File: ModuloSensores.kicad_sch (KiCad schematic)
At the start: 12 parts, among them J27 Borner Ctrl. Empot. 1, J28 Borner Ctrl. Empot. 2, J29 Borner Ctrl. Polea, J30 Borner Capacitor 1, J31 Borner Capacitor 2, Q1 2N222, SW2 SW_SPDT, SW3 SW_SPDT, SW4 SW_SPDT

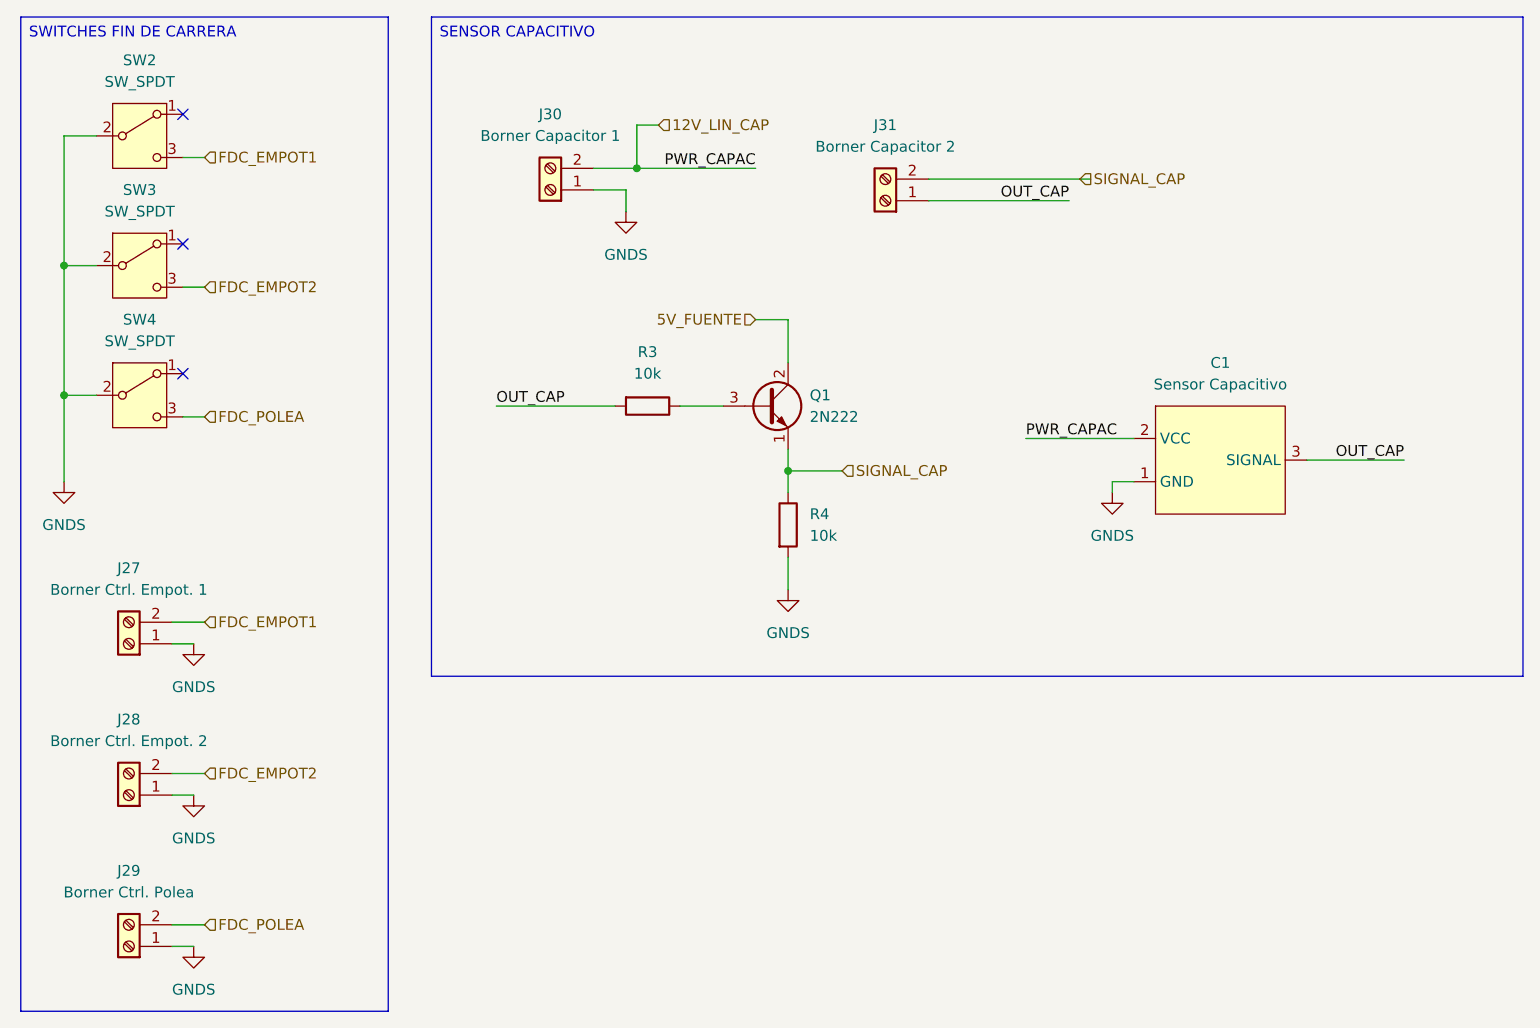
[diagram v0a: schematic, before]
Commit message: Version mandada para PCB
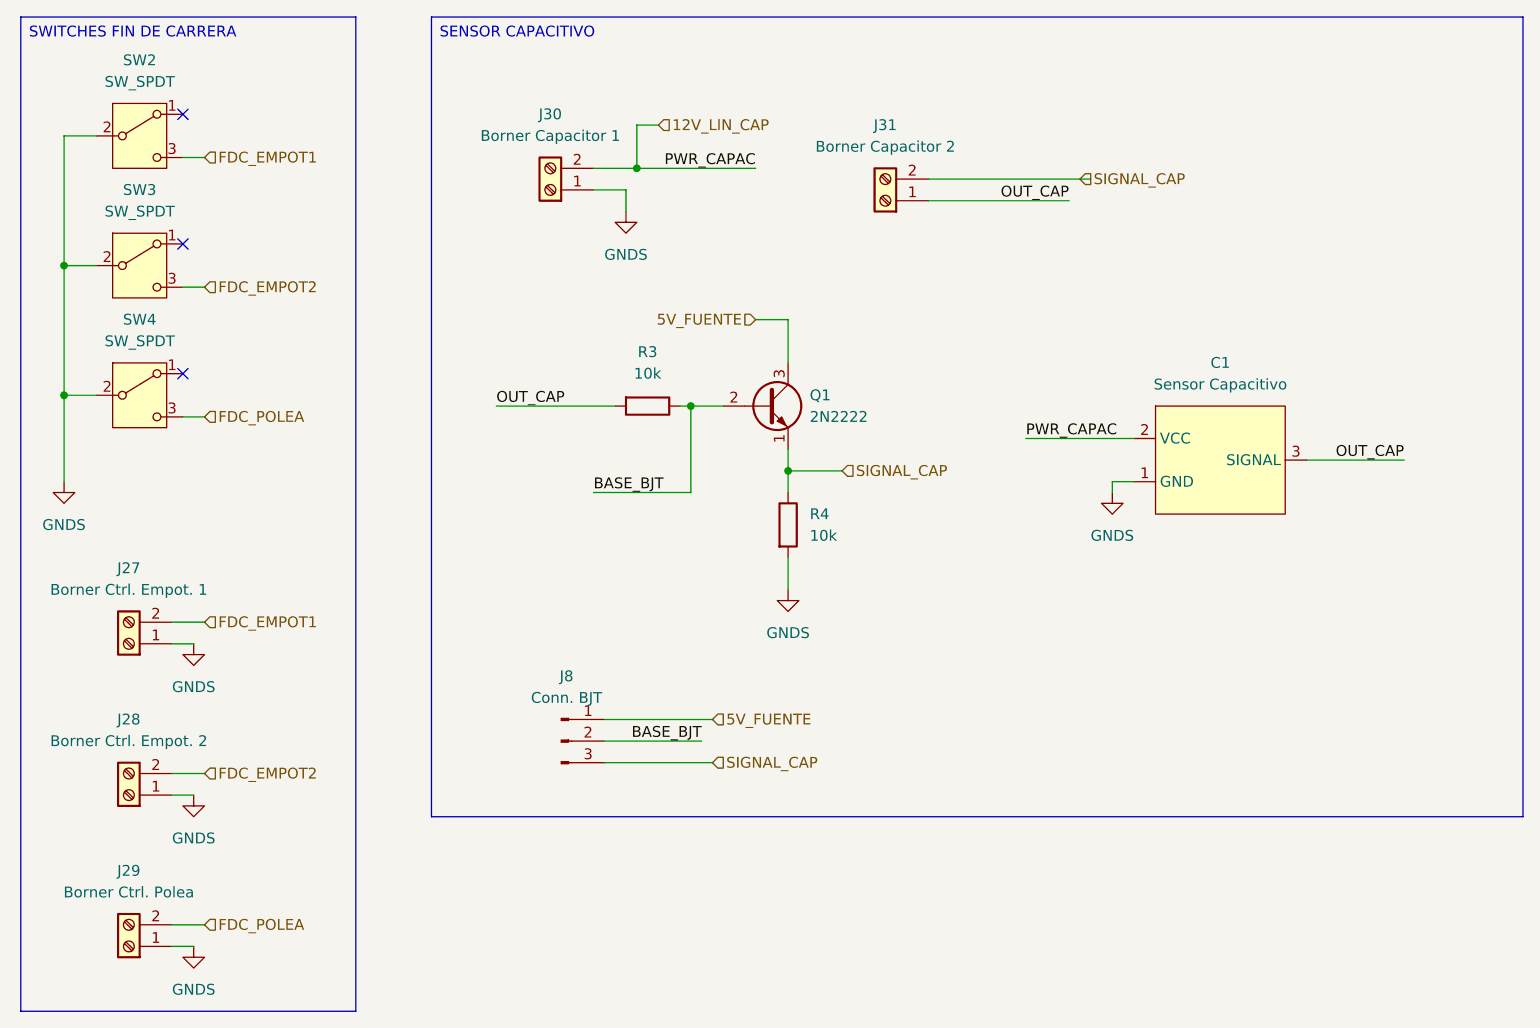
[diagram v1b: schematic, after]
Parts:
- removed Q1: 2N222, Package_TO_SOT_THT:TO-126-3_Vertical, symbol Transistor_BJT:BF457
- added J8: Conn. BJT, Connector_PinHeader_2.54mm:PinHeader_1x03_P2.54mm_Vertical, symbol Connector:Conn_01x03_Pin
- added Q1: 2N2222, Package_TO_SOT_THT:TO-92_Inline, symbol Transistor_BJT:2N3904
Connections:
- net 5V_FUENTE: now also J8.1 (Pin_1), Q1.3 (C)
- net SIGNAL_CAP: now also J8.3 (Pin_3), Q1.1 (E)
- net BASE_BJT: now reaches R3.1
- net BASE_BJT: now also J8.2 (Pin_2), Q1.2 (B)
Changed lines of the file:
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@@
 		(exclude_from_sim no)
 		(at 16.51 16.51 0)
-		(size 43.18 116.84)
+		(size 39.37 116.84)
 		(margins 0.9525 0.9525 0.9525 0.9525)
 		(stroke
@@
 		(exclude_from_sim no)
 		(at 64.77 16.51 0)
-		(size 128.27 77.47)
+		(size 128.27 93.98)
 		(margins 0.9525 0.9525 0.9525 0.9525)
 		(stroke
@@
 	)
 	(junction
+		(at 95.25 62.23)
+		(diameter 0)
+		(color 0 0 0 0)
+	)
+	(junction
 		(at 21.59 60.96)
 		(diameter 0)
@@
 	(wire
 		(pts
-			(xy 99.06 62.23) (xy 93.98 62.23)
+			(xy 95.25 62.23) (xy 95.25 72.39)
+		)
+		(stroke
+			(width 0)
+			(type default)
+		)
+	)
+	(wire
+		(pts
+			(xy 99.06 62.23) (xy 95.25 62.23)
 		)
 		(stroke
@@
 	(wire
 		(pts
+			(xy 85.09 104.14) (xy 97.79 104.14)
+		)
+		(stroke
+			(width 0)
+			(type default)
+		)
+	)
+	(wire
+		(pts
 			(xy 21.59 45.72) (xy 25.4 45.72)
 		)
@@
 	(wire
 		(pts
+			(xy 85.09 99.06) (xy 97.79 99.06)
+		)
+		(stroke
+			(width 0)
+			(type default)
+		)
+	)
+	(wire
+		(pts
 			(xy 34.29 125.73) (xy 36.83 125.73)
 		)
@@
 	(wire
 		(pts
+			(xy 85.09 101.6) (xy 96.52 101.6)
+		)
+		(stroke
+			(width 0)
+			(type default)
+		)
+	)
+	(wire
+		(pts
 			(xy 134.62 66.04) (xy 147.32 66.04)
 		)
@@
 	(wire
 		(pts
+			(xy 95.25 62.23) (xy 93.98 62.23)
+		)
+		(stroke
+			(width 0)
+			(type default)
+		)
+	)
+	(wire
+		(pts
 			(xy 35.56 48.26) (xy 38.1 48.26)
 		)
@@
 			(width 0)
 			(type default)
+		)
+	)
+	(wire
+		(pts
+			(xy 83.82 72.39) (xy 95.25 72.39)
+		)
+		(stroke
+			(width 0)
+			(type default)
+		)
+	)
+	(label "BASE_BJT"
+		(at 96.52 101.6 180)
+		(effects
+			(font
+				(size 1.27 1.27)
+			)
+			(justify right bottom)
 		)
 	)
@@
 	(label "PWR_CAPAC"
 		(at 134.62 66.04 0)
+		(effects
+			(font
+				(size 1.27 1.27)
+			)
+			(justify left bottom)
+		)
+	)
+	(label "BASE_BJT"
+		(at 83.82 72.39 0)
 		(effects
 			(font
@@
 		(shape input)
 		(at 113.03 69.85 0)
+		(effects
+			(font
+				(size 1.27 1.27)
+			)
+			(justify left)
+		)
+	)
+	(hierarchical_label "SIGNAL_CAP"
+		(shape input)
+		(at 97.79 104.14 0)
+		(effects
+			(font
+				(size 1.27 1.27)
+			)
+			(justify left)
+		)
+	)
+	(hierarchical_label "5V_FUENTE"
+		(shape input)
+		(at 97.79 99.06 0)
 		(effects
 			(font
@@
 	)
 	(symbol
+		(lib_id "Transistor_BJT:2N3904")
+		(at 104.14 62.23 0)
+		(unit 1)
+		(exclude_from_sim no)
+		(in_bom yes)
+		(on_board no)
+		(dnp no)
+		(fields_autoplaced yes)
+		(property "Reference" "Q1"
+			(at 109.22 60.9599 0)
+			(effects
+				(font
+					(size 1.27 1.27)
+				)
+				(justify left)
+			)
+		)
+		(property "Value" "2N2222"
+			(at 109.22 63.4999 0)
+			(effects
+				(font
+					(size 1.27 1.27)
+				)
+				(justify left)
+			)
+		)
+		(property "Footprint" "Package_TO_SOT_THT:TO-92_Inline"
+			(at 109.22 64.135 0)
+			(effects
+				(font
+					(size 1.27 1.27)
+					(italic yes)
+				)
+				(justify left)
+				(hide yes)
+			)
+		)
+		(property "Datasheet" "https://www.onsemi.com/pub/Collateral/2N3903-D.PDF"
+			(at 104.14 62.23 0)
+			(effects
+				(font
+					(size 1.27 1.27)
+				)
+				(justify left)
+				(hide yes)
+			)
+		)
+		(property "Description" "0.2A Ic, 40V Vce, Small Signal NPN Transistor, TO-92"
+			(at 104.14 62.23 0)
+			(effects
+				(font
+					(size 1.27 1.27)
+				)
+				(hide yes)
+			)
+		)
+		(pin "2"
+		)
+		(pin "3"
+		)
+		(pin "1"
+		)
+		(instances
+			(project ""
+				(path "/911418d1-1173-4b7a-bef0-90371fdba379/78986bcd-9b0f-4d22-8a2b-9ff24fa4d941"
+					(reference "Q1")
+					(unit 1)
+				)
+			)
+		)
+	)
+	(symbol
 		(lib_id "Connector:Screw_Terminal_01x02")
 		(at 118.11 38.1 180)
@@
 	)
 	(symbol
+		(lib_id "Connector:Conn_01x03_Pin")
+		(at 80.01 101.6 0)
+		(unit 1)
+		(exclude_from_sim no)
+		(in_bom yes)
+		(on_board yes)
+		(dnp no)
+		(fields_autoplaced yes)
+		(property "Reference" "J8"
+			(at 80.645 93.98 0)
+			(effects
+				(font
+					(size 1.27 1.27)
+				)
+			)
+		)
+		(property "Value" "Conn. BJT"
+			(at 80.645 96.52 0)
+			(effects
+				(font
+					(size 1.27 1.27)
+				)
+			)
+		)
+		(property "Footprint" "Connector_PinHeader_2.54mm:PinHeader_1x03_P2.54mm_Vertical"
+			(at 80.01 101.6 0)
+			(effects
+				(font
+					(size 1.27 1.27)
+				)
+				(hide yes)
+			)
+		)
+		(property "Datasheet" "~"
+			(at 80.01 101.6 0)
+			(effects
+				(font
+					(size 1.27 1.27)
+				)
+				(hide yes)
+			)
+		)
+		(property "Description" "Generic connector, single row, 01x03, script generated"
+			(at 80.01 101.6 0)
+			(effects
+				(font
+					(size 1.27 1.27)
+				)
+				(hide yes)
+			)
+		)
+		(pin "1"
+		)
+		(pin "2"
+		)
+		(pin "3"
+		)
+		(instances
+			(project ""
+				(path "/911418d1-1173-4b7a-bef0-90371fdba379/78986bcd-9b0f-4d22-8a2b-9ff24fa4d941"
+					(reference "J8")
+					(unit 1)
+				)
+			)
+		)
+	)
+	(symbol
 		(lib_id "power:GNDS")
 		(at 36.83 107.95 0)
@@
 					(unit 1)
 				)
-			)
-		)
-	)
-	(symbol
-		(lib_id "Transistor_BJT:BF457")
-		(at 104.14 62.23 0)
-		(unit 1)
-		(exclude_from_sim no)
-		(in_bom yes)
-		(on_board yes)
-		(dnp no)
-		(fields_autoplaced yes)
-		(property "Reference" "Q1"
-			(at 109.22 60.9599 0)
-			(effects
-				(font
-					(size 1.27 1.27)
-				)
-				(justify left)
-			)
-		)
-		(property "Value" "2N222"
-			(at 109.22 63.4999 0)
-			(effects
-				(font
-					(size 1.27 1.27)
-				)
-				(justify left)
-			)
-		)
-		(property "Footprint" "Package_TO_SOT_THT:TO-126-3_Vertical"
-			(at 109.22 64.135 0)
-			(effects
-				(font
-					(size 1.27 1.27)
-					(italic yes)
-				)
-				(justify left)
-				(hide yes)
-			)
-		)
-		(property "Datasheet" "https://www.pcpaudio.com/pcpfiles/transistores/BF457-8-9.pdf"
-			(at 104.14 62.23 0)
-			(effects
-				(font
-					(size 1.27 1.27)
-				)
-				(justify left)
-				(hide yes)
-			)
-		)
-		(property "Description" "0.1A Ic, 160V Vce, High Voltage NPN Transistor, TO-126"
-			(at 104.14 62.23 0)
-			(effects
-				(font
-					(size 1.27 1.27)
-				)
-				(hide yes)
-			)
-		)
-		(pin "2"
-		)
-		(pin "1"
-		)
-		(pin "3"
-		)
-		(instances
-			(project ""
-				(path "/911418d1-1173-4b7a-bef0-90371fdba379/78986bcd-9b0f-4d22-8a2b-9ff24fa4d941"
-					(reference "Q1")
-					(unit 1)
-				)
